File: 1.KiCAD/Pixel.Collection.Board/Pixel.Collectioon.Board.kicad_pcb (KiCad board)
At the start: 4 copper layers, 299.7 x 452.1 mm, 75 parts

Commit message: Refilled Copper Zones
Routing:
- net unconnected-(CH14-Pad1): track 262.1 -> 266.9 mm
- net unconnected-(CH3-Pad1): track 186.6 -> 189.0 mm
- net unconnected-(CH16-Pad1): track 726.6 -> 724.2 mm
- net unconnected-(CH9-Pad1): track 171.0 -> 172.7 mm
- net unconnected-(CH6-Pad1): track 253.7 -> 252.9 mm

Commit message: Minor Changes
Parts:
- removed ? (x8): , 
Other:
- outline, holes or cut-outs redrawn

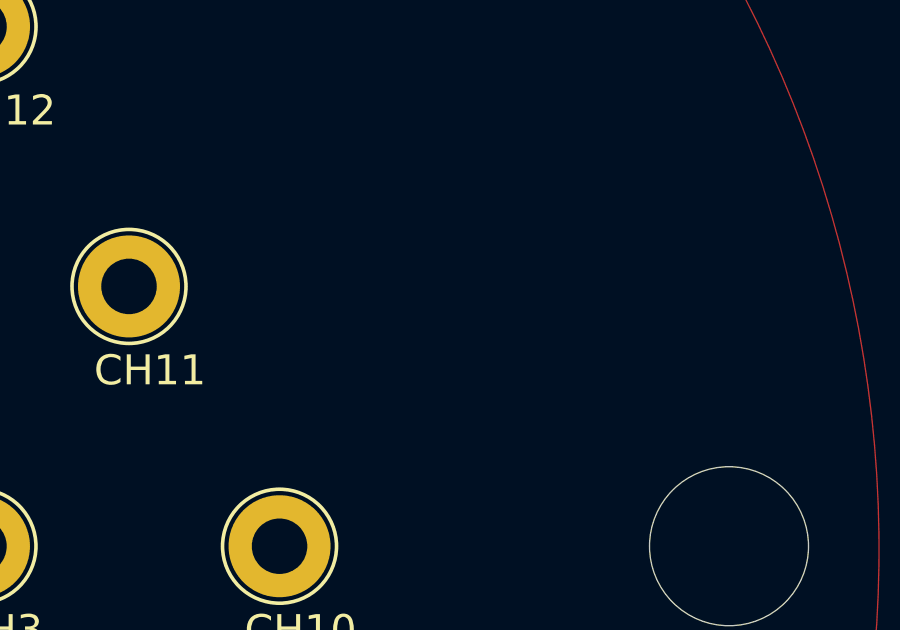
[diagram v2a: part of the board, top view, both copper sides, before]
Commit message: Spaced collection board traces
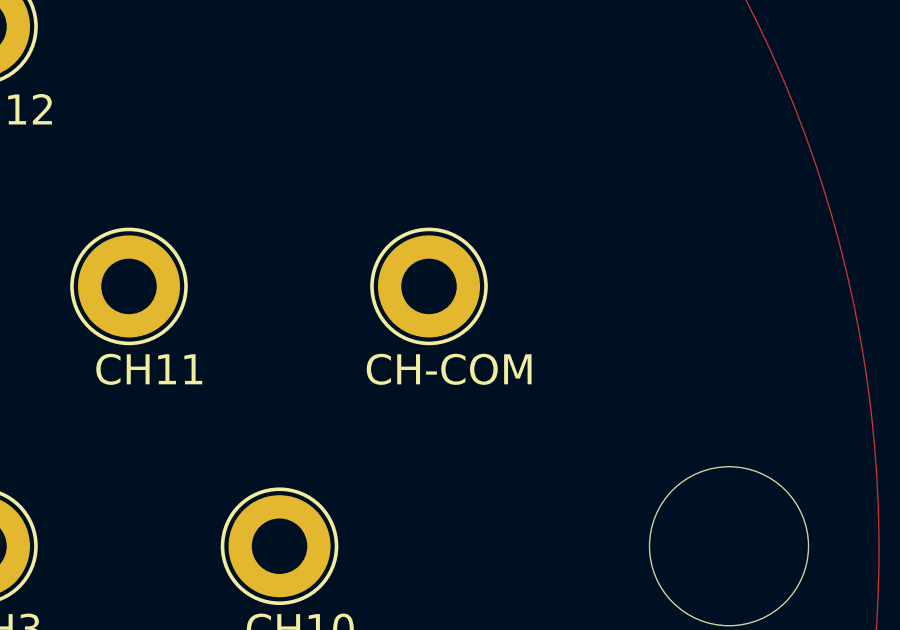
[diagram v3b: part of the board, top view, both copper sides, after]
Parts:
- added CH-COM: READOUT, TestPoint:TestPoint_Loop_D2.50mm_Drill1.85mm, F.Cu at (174.9, 122.2)
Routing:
- net unconnected-(CH11-Pad1): track 216.0 -> 350.7 mm
- net unconnected-(CH16-Pad1): track 724.2 -> 606.8 mm
- net unconnected-(CH6-Pad1): track 252.9 -> 174.1 mm
- net unconnected-(CH15-Pad1): track 254.6 -> 203.7 mm
- net unconnected-(CH5-Pad1): track 154.3 -> 200.9 mm
- net unconnected-(CH14-Pad1): track 266.9 -> 226.9 mm
- net unconnected-(CH7-Pad1): track 202.8 -> 162.9 mm
- net unconnected-(CH9-Pad1): track 172.7 -> 141.9 mm
- net unconnected-(CH12-Pad1): track 232.1 -> 204.3 mm
- net unconnected-(CH3-Pad1): track 189.0 -> 163.2 mm
- net unconnected-(CH10-Pad1): track 185.5 -> 159.9 mm
- net unconnected-(CH8-Pad1): track 149.9 -> 132.1 mm
- net unconnected-(CH4-Pad1): track 176.4 -> 161.4 mm
- net unconnected-(CH13-Pad1): track 240.1 -> 228.6 mm
- net unconnected-(CH1-Pad1): track 153.8 -> 158.0 mm
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
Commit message: Thickened ground traces and updated channel wires
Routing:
- net unconnected-(CH7-Pad1): track 162.9 -> 156.5 mm
- net unconnected-(CH16-Pad1): track 606.8 -> 601.2 mm
- net unconnected-(CH5-Pad1): track 200.9 -> 199.3 mm
- net unconnected-(CH15-Pad1): track 203.7 -> 202.2 mm
- net unconnected-(CH6-Pad1): track 174.1 -> 172.6 mm
- net unconnected-(CH1-Pad1): track 158.0 -> 156.7 mm
- net unconnected-(CH2-Pad1): track 146.6 -> 146.1 mm

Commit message: A
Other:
- board text added: "C"
- board text added: "ch1"
- board text added: "ch10"
- board text added: "ch11"
- board text added: "ch12"
- board text added: "ch13"
- board text added: "ch14"
- board text added: "ch15"
- board text added: "ch16"
- board text added: "ch17"
- board text added: "ch18"
- board text added: "ch19"
- board text added: "ch2"
- board text added: "ch3"
- board text added: "ch4"
- board text added: "ch5"
- board text added: "ch6"
- board text added: "ch7"
- board text added: "ch8"
- board text added: "ch9"
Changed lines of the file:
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@@
     )
     (pad_to_mask_clearance 0)
+    (aux_axis_origin 149.86 130.81)
     (pcbplotparams
       (layerselection 0x00010fc_ffffffff)
@@
   (gr_rect (start 33.147 266.954) (end 266.573 439.674)
     (stroke (width 0.15) (type solid)) (fill none) (layer "User.9"))
+  (gr_text "ch17" (at 102.335 279.955) (layer "User.7")
+    (effects (font (size 1.5 1.5) (thickness 0.3) bold) (justify left bottom))
+  )
+  (gr_text "C" (at 203.595 279.945) (layer "User.7")
+    (effects (font (size 1.5 1.5) (thickness 0.3) bold) (justify left bottom))
+  )
+  (gr_text "ch11" (at 195.775 277.075) (layer "User.7")
+    (effects (font (size 1.5 1.5) (thickness 0.3) bold) (justify left bottom))
+  )
+  (gr_text "ch6" (at 96.7 277.595) (layer "User.7")
+    (effects (font (size 1.5 1.5) (thickness 0.3) bold) (justify left bottom))
+  )
+  (gr_text "ch8" (at 156.91 279.385) (layer "User.7")
+    (effects (font (size 1.5 1.5) (thickness 0.3) bold) (justify left bottom))
+  )
+  (gr_text "ch16" (at 91.08 280.08) (layer "User.7")
+    (effects (font (size 1.5 1.5) (thickness 0.3) bold) (justify left bottom))
+  )
+  (gr_text "ch18" (at 124.075 276.505) (layer "User.7")
+    (effects (font (size 1.5 1.5) (thickness 0.3) bold) (justify left bottom))
+  )
+  (gr_text "ch7" (at 119.05 279.855) (layer "User.7")
+    (effects (font (size 1.5 1.5) (thickness 0.3) bold) (justify left bottom))
+  )
+  (gr_text "ch13" (at 63.505 277.085) (layer "User.7")
+    (effects (font (size 1.5 1.5) (thickness 0.3) bold) (justify left bottom))
+  )
+  (gr_text "ch15" (at 69.295 279.83) (layer "User.7")
+    (effects (font (size 1.5 1.5) (thickness 0.3) bold) (justify left bottom))
+  )
+  (gr_text "ch9" (at 166.5 279.86) (layer "User.7")
+    (effects (font (size 1.5 1.5) (thickness 0.3) bold) (justify left bottom))
+  )
+  (gr_text "ch1" (at 129.62 279.56) (layer "User.7")
+    (effects (font (size 1.5 1.5) (thickness 0.3) bold) (justify left bottom))
+  )
+  (gr_text "ch4" (at 161.685 277.18) (layer "User.7")
+    (effects (font (size 1.5 1.5) (thickness 0.3) bold) (justify left bottom))
+  )
+  (gr_text "ch12" (at 208.72 277.2) (layer "User.7")
+    (effects (font (size 1.5 1.5) (thickness 0.3) bold) (justify left bottom))
+  )
+  (gr_text "ch19" (at 134.09 276.87) (layer "User.7")
+    (effects (font (size 1.5 1.5) (thickness 0.3) bold) (justify left bottom))
+  )
+  (gr_text "ch14" (at 58.025 279.93) (layer "User.7")
+    (effects (font (size 1.5 1.5) (thickness 0.3) bold) (justify left bottom))
+  )
+  (gr_text "ch5" (at 85.63 277.485) (layer "User.7")
+    (effects (font (size 1.5 1.5) (thickness 0.3) bold) (justify left bottom))
+  )
+  (gr_text "ch3" (at 171.45 277.08) (layer "User.7")
+    (effects (font (size 1.5 1.5) (thickness 0.3) bold) (justify left bottom))
+  )
+  (gr_text "ch2" (at 139.315 279.405) (layer "User.7")
+    (effects (font (size 1.5 1.5) (thickness 0.3) bold) (justify left bottom))
+  )
+  (gr_text "ch10" (at 176.63 280.165) (layer "User.7")
+    (effects (font (size 1.5 1.5) (thickness 0.3) bold) (justify left bottom))
+  )
   (segment (start 149.857923 141.172077) (end 149.857923 130.81) (width 0.25) (layer "In2.Cu") (net 2))
   (segment (start 145.035 149.445) (end 145.035 145.995) (width 0.25) (layer "In2.Cu") (net 2))

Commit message: Started Designing Vessel. Minor Updates
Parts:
- removed H10, H11, H12, H13, H14, H15, H16, H17, H18, H19, H20, H21, H22, H23, H5, H6, H7, H8, H9: MountingHole_Pad, MountingHole:MountingHole_5.3mm_M5_DIN965_Pad
- added H25: MountingHole_Pad, MountingHole:MountingHole_5.3mm_M5_DIN965_Pad, F.Cu at (264.6, 93.5)
- added H26: MountingHole_Pad, MountingHole:MountingHole_5.3mm_M5_DIN965_Pad, F.Cu at (247.5, 59.9)
- added H27: MountingHole_Pad, MountingHole:MountingHole_5.3mm_M5_DIN965_Pad, F.Cu at (220.8, 33.2)
- added H28: MountingHole_Pad, MountingHole:MountingHole_5.3mm_M5_DIN965_Pad, F.Cu at (187.1, 16.1)
- added H29: MountingHole_Pad, MountingHole:MountingHole_5.3mm_M5_DIN965_Pad, F.Cu at (149.9, 10.2)
- added H30: MountingHole_Pad, MountingHole:MountingHole_5.3mm_M5_DIN965_Pad, F.Cu at (112.6, 16.1)
- added H31: MountingHole_Pad, MountingHole:MountingHole_5.3mm_M5_DIN965_Pad, F.Cu at (78.9, 33.2)
- added H32: MountingHole_Pad, MountingHole:MountingHole_5.3mm_M5_DIN965_Pad, F.Cu at (52.3, 59.9)
- added H33: MountingHole_Pad, MountingHole:MountingHole_5.3mm_M5_DIN965_Pad, F.Cu at (35.1, 93.5)
- added H34: MountingHole_Pad, MountingHole:MountingHole_5.3mm_M5_DIN965_Pad, F.Cu at (29.2, 130.8)
- added H35: MountingHole_Pad, MountingHole:MountingHole_5.3mm_M5_DIN965_Pad, F.Cu at (35.1, 168.1)
- added H36: MountingHole_Pad, MountingHole:MountingHole_5.3mm_M5_DIN965_Pad, F.Cu at (52.3, 201.7)
- added H37: MountingHole_Pad, MountingHole:MountingHole_5.3mm_M5_DIN965_Pad, F.Cu at (78.9, 228.4)
- added H38: MountingHole_Pad, MountingHole:MountingHole_5.3mm_M5_DIN965_Pad, F.Cu at (112.6, 245.6)
- added H39: MountingHole_Pad, MountingHole:MountingHole_5.3mm_M5_DIN965_Pad, F.Cu at (149.9, 251.5)
- added H40: MountingHole_Pad, MountingHole:MountingHole_5.3mm_M5_DIN965_Pad, F.Cu at (187.1, 245.6)
- added H41: MountingHole_Pad, MountingHole:MountingHole_5.3mm_M5_DIN965_Pad, F.Cu at (220.8, 228.4)
- added H42: MountingHole_Pad, MountingHole:MountingHole_5.3mm_M5_DIN965_Pad, F.Cu at (247.5, 201.7)
- added H43: MountingHole_Pad, MountingHole:MountingHole_5.3mm_M5_DIN965_Pad, F.Cu at (264.6, 168.1)
